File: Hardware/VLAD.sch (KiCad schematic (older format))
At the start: 29 parts, among them J1 BMP388, J2 BNO055, Q1 S8050, Q2 S8050, SW1 SW_Push, SW2 SW_Push, U1 ESP32-WROOM-32

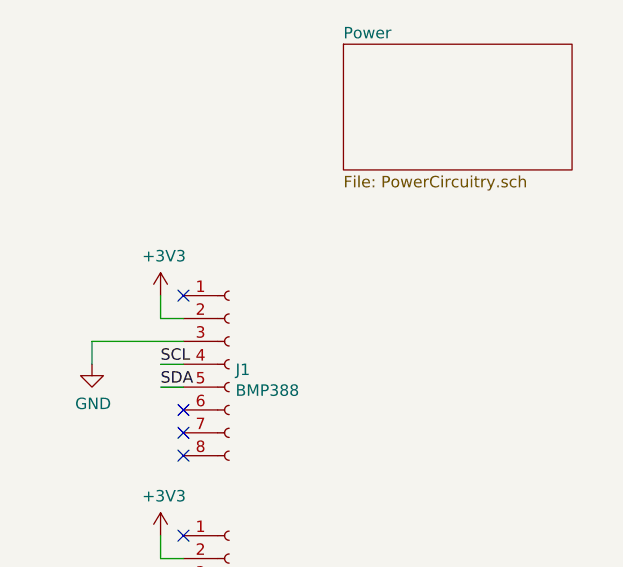
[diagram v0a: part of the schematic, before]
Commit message: Need to change pin headers for servo
Unsure at this stage, will look into which transistors etc to use.
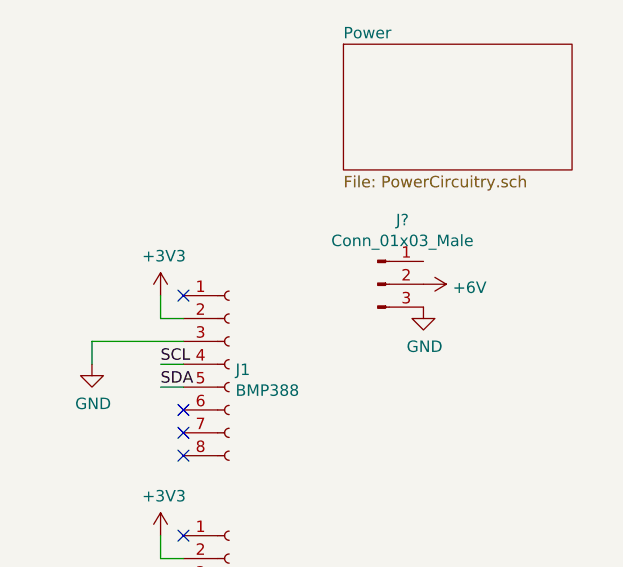
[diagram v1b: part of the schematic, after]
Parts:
- added J?: Conn_01x03_Male, symbol Connector:Conn_01x03_Male
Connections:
- net GND: now also J?.3 (Pin_3)
- new net +6V: J?.2 (Pin_2)
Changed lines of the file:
@@
 NoConn ~ 6750 4850
 NoConn ~ 7050 3950
+$Comp
+L power:+6V #PWR?
+U 1 1 60A0C2D4
+P 10200 2100
+F 0 "#PWR?" H 10200 1950 50  0001 C CNN
+F 1 "+6V" V 10215 2228 50  0000 L CNN
+F 2 "" H 10200 2100 50  0001 C CNN
+F 3 "" H 10200 2100 50  0001 C CNN
+	1    10200 2100
+	0    1    1    0
+$EndComp
+$Comp
+L power:GND #PWR?
+U 1 1 60A0B510
+P 10200 2200
+F 0 "#PWR?" H 10200 1950 50  0001 C CNN
+F 1 "GND" H 10205 2027 50  0000 C CNN
+F 2 "" H 10200 2200 50  0001 C CNN
+F 3 "" H 10200 2200 50  0001 C CNN
+	1    10200 2200
+	1    0    0    -1
+$EndComp
+$Comp
+L Connector:Conn_01x03_Male J?
+U 1 1 60A0527F
+P 10000 2100
+F 0 "J?" H 10108 2381 50  0000 C CNN
+F 1 "Conn_01x03_Male" H 10108 2290 50  0000 C CNN
+F 2 "" H 10000 2100 50  0001 C CNN
+F 3 "~" H 10000 2100 50  0001 C CNN
+	1    10000 2100
+	1    0    0    -1
+$EndComp
 $EndSCHEMATC

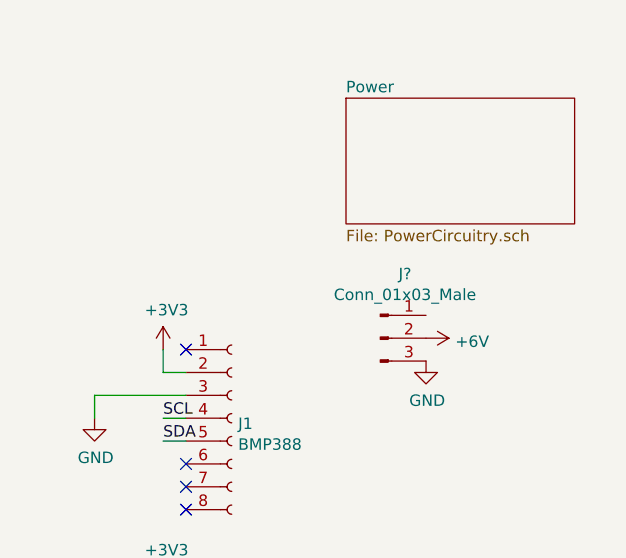
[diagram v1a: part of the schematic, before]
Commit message: Split PCB setup
Setup the PCB with each section split. J5 didn't have a schematic so I picked one.
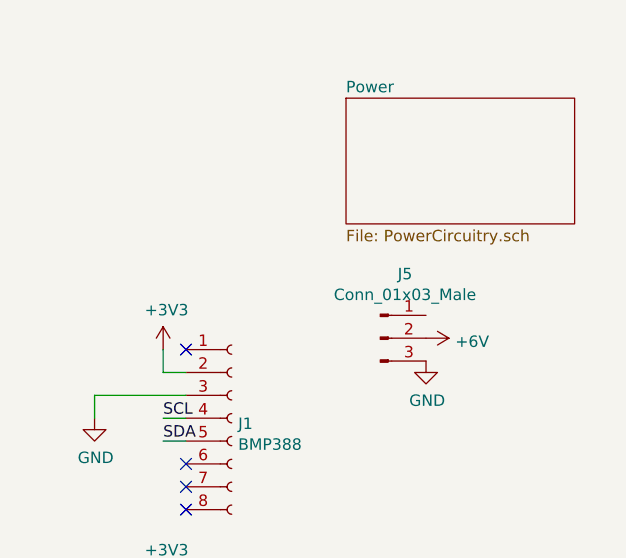
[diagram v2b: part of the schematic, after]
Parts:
- J5: renamed from J?; footprint (none) -> Connector_PinHeader_2.54mm:PinHeader_1x03_P2.54mm_Vertical
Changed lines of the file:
@@
 EESchema Schematic File Version 4
-LIBS:VLAD-cache
 EELAYER 30 0
 EELAYER END
@@
 NoConn ~ 7050 3950
 $Comp
-L power:+6V #PWR?
+L power:+6V #PWR0102
 U 1 1 60A0C2D4
 P 10200 2100
-F 0 "#PWR?" H 10200 1950 50  0001 C CNN
+F 0 "#PWR0102" H 10200 1950 50  0001 C CNN
 F 1 "+6V" V 10215 2228 50  0000 L CNN
 F 2 "" H 10200 2100 50  0001 C CNN
@@
 $EndComp
 $Comp
-L power:GND #PWR?
+L power:GND #PWR0103
 U 1 1 60A0B510
 P 10200 2200
-F 0 "#PWR?" H 10200 1950 50  0001 C CNN
+F 0 "#PWR0103" H 10200 1950 50  0001 C CNN
 F 1 "GND" H 10205 2027 50  0000 C CNN
 F 2 "" H 10200 2200 50  0001 C CNN
@@
 $EndComp
 $Comp
-L Connector:Conn_01x03_Male J?
+L Connector:Conn_01x03_Male J5
 U 1 1 60A0527F
 P 10000 2100
-F 0 "J?" H 10108 2381 50  0000 C CNN
+F 0 "J5" H 10108 2381 50  0000 C CNN
 F 1 "Conn_01x03_Male" H 10108 2290 50  0000 C CNN
-F 2 "" H 10000 2100 50  0001 C CNN
+F 2 "Connector_PinHeader_2.54mm:PinHeader_1x03_P2.54mm_Vertical" H 10000 2100 50  0001 C CNN
 F 3 "~" H 10000 2100 50  0001 C CNN
 	1    10000 2100

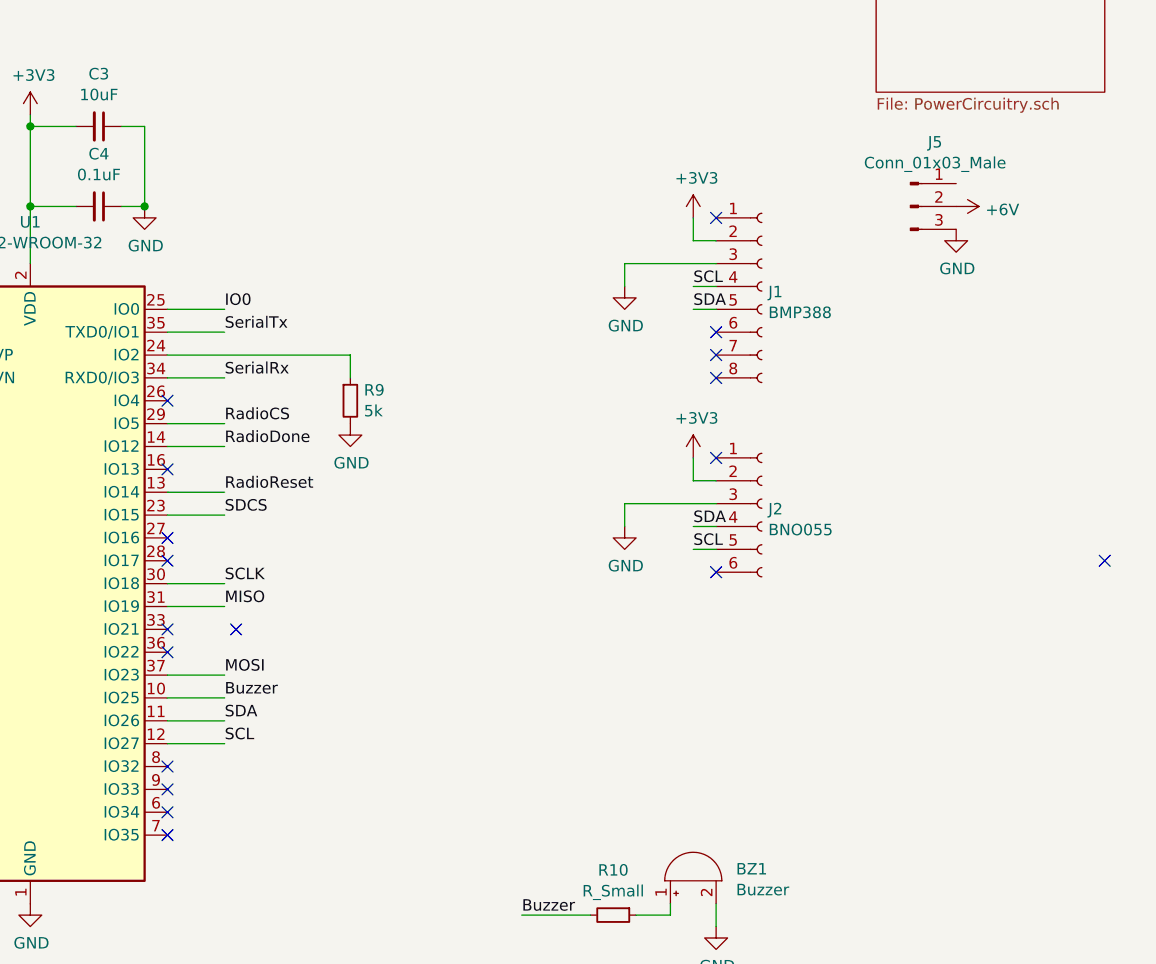
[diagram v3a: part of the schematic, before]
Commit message: Fixed N-Channel MOSFET, etc
And a few net label tings
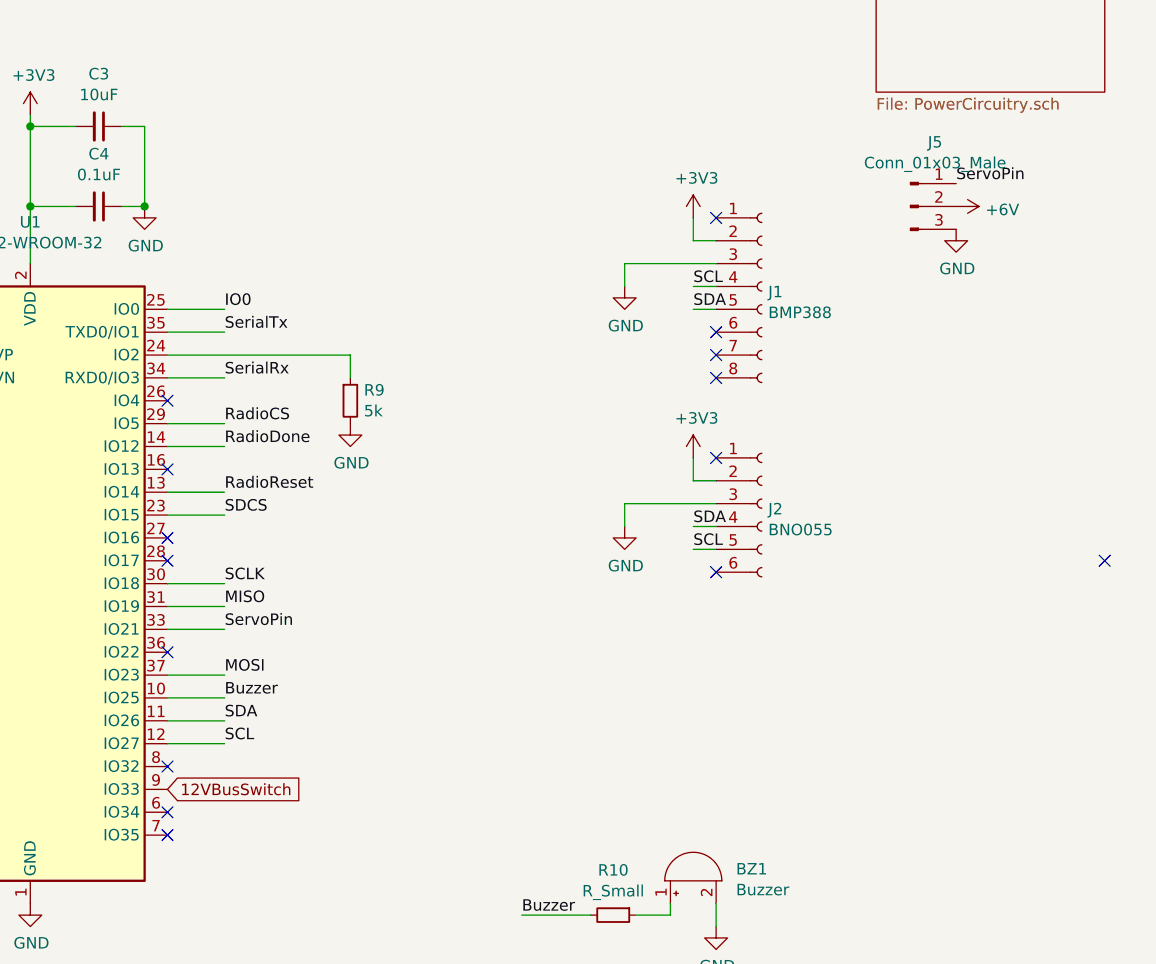
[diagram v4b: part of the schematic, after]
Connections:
- net ServoPin: now reaches U1.33 (IO21)
- net ServoPin: now also J5.1 (Pin_1)
- net 12VBusSwitch: now reaches U1.9 (IO33)
- no-connect marks 26 -> 23
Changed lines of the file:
@@
 $EndDescr
-$Comp
-L VLAD-rescue:ESP32-WROOM-32-RF_Module U1
-U 1 1 6068A42E
-P 6150 3750
-F 0 "U1" H 6150 5331 50  0000 C CNN
-F 1 "ESP32-WROOM-32" H 6150 5240 50  0000 C CNN
-F 2 "RF_Module:ESP32-WROOM-32" H 6150 2250 50  0001 C CNN
-F 3 "https://www.espressif.com/sites/default/files/documentation/esp32-wroom-32_datasheet_en.pdf" H 5850 3800 50  0001 C CNN
-	1    6150 3750
-	1    0    0    -1
-$EndComp
 $Comp
 L power:GND #PWR07
@@
 	1    0    0    -1
 $EndComp
-Wire Wire Line
-	6750 3750 7000 3750
-Wire Wire Line
-	6750 3850 7000 3850
-Wire Wire Line
-	6750 4150 7000 4150
 $Sheet
 S 800  1750 550  550
@@
 Text Label 1450 1000 0    50   ~ 0
 MOSI
-Wire Wire Line
-	6750 3150 7000 3150
 Text Label 7000 3150 0    50   ~ 0
 RadioDone
 Text Label 1450 1400 0    50   ~ 0
 RadioDone
-Wire Wire Line
-	6750 3350 7000 3350
 Text Label 7000 3350 0    50   ~ 0
 RadioReset
-Wire Wire Line
-	6750 3050 7000 3050
 Text Label 7000 3050 0    50   ~ 0
 RadioCS
@@
 Text Label 1450 2200 0    50   ~ 0
 SDCS
-Wire Wire Line
-	6750 3450 7000 3450
 Text Label 7000 3450 0    50   ~ 0
 SDCS
-Wire Wire Line
-	6750 2750 7550 2750
 Wire Wire Line
 	7550 2750 7550 2850
@@
 Wire Wire Line
 	6650 1750 6650 2100
-Wire Wire Line
-	6750 2850 7000 2850
-Wire Wire Line
-	6750 2650 7000 2650
 Text Label 7000 2850 0    50   ~ 0
 SerialRx
@@
 Text Label 8300 5200 0    50   ~ 0
 Buzzer
-Wire Wire Line
-	6750 4250 7000 4250
 Text Label 7000 4250 0    50   ~ 0
 Buzzer
-Wire Wire Line
-	6750 4350 7000 4350
-Wire Wire Line
-	6750 4450 7000 4450
 Text Label 7000 4350 0    50   ~ 0
 SDA
@@
 NoConn ~ 6750 3550
 NoConn ~ 6750 3650
-NoConn ~ 6750 3950
 NoConn ~ 6750 4050
-NoConn ~ 6750 4550
-NoConn ~ 6750 4650
-NoConn ~ 6750 4750
 NoConn ~ 6750 4850
-NoConn ~ 7050 3950
 $Comp
 L power:+6V #PWR0102
@@
 	1    0    0    -1
 $EndComp
+Wire Wire Line
+	6750 4450 7000 4450
+Wire Wire Line
+	6750 4350 7000 4350
+Wire Wire Line
+	6750 4250 7000 4250
+Wire Wire Line
+	6750 4150 7000 4150
+Wire Wire Line
+	6750 3850 7000 3850
+Wire Wire Line
+	6750 3750 7000 3750
+Wire Wire Line
+	6750 3450 7000 3450
+Wire Wire Line
+	6750 3350 7000 3350
+Wire Wire Line
+	6750 3150 7000 3150
+Wire Wire Line
+	6750 3050 7000 3050
+Wire Wire Line
+	6750 2850 7000 2850
+Wire Wire Line
+	6750 2750 7550 2750
+Wire Wire Line
+	6750 2650 7000 2650
+NoConn ~ 6750 4550
+$Comp
+L VLAD-rescue:ESP32-WROOM-32-RF_Module U1
+U 1 1 6068A42E
+P 6150 3750
+F 0 "U1" H 6150 5331 50  0000 C CNN
+F 1 "ESP32-WROOM-32" H 6150 5240 50  0000 C CNN
+F 2 "RF_Module:ESP32-WROOM-32" H 6150 2250 50  0001 C CNN
+F 3 "https://www.espressif.com/sites/default/files/documentation/esp32-wroom-32_datasheet_en.pdf" H 5850 3800 50  0001 C CNN
+	1    6150 3750
+	1    0    0    -1
+$EndComp
+Text GLabel 6750 4650 2    50   Input ~ 0
+12VBusSwitch
+NoConn ~ 6750 4750
+Text Label 7000 3950 0    50   ~ 0
+ServoPin
+Text Label 10200 2000 0    50   ~ 0
+ServoPin
+Wire Wire Line
+	6750 3950 7000 3950
 $EndSCHEMATC

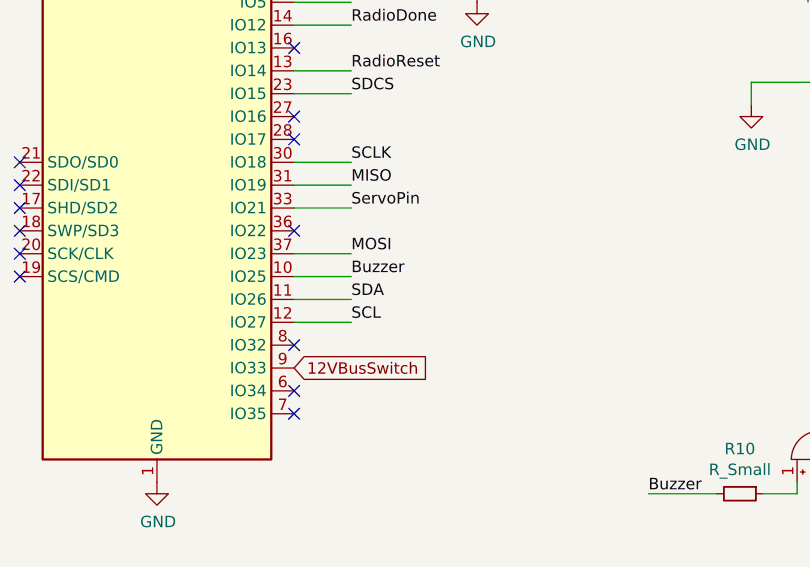
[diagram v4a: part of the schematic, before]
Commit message: Tracks done (albeit OCDifying)
All tracks are done in the sense that everything has found a routing, some components still may need to be moved though, such as the sensors on board and the push switches. 
Antenna stuff needs doing.
Board may need to be reshaped (keepout zone?).
GND plane needs to be added + silkscreens + memes
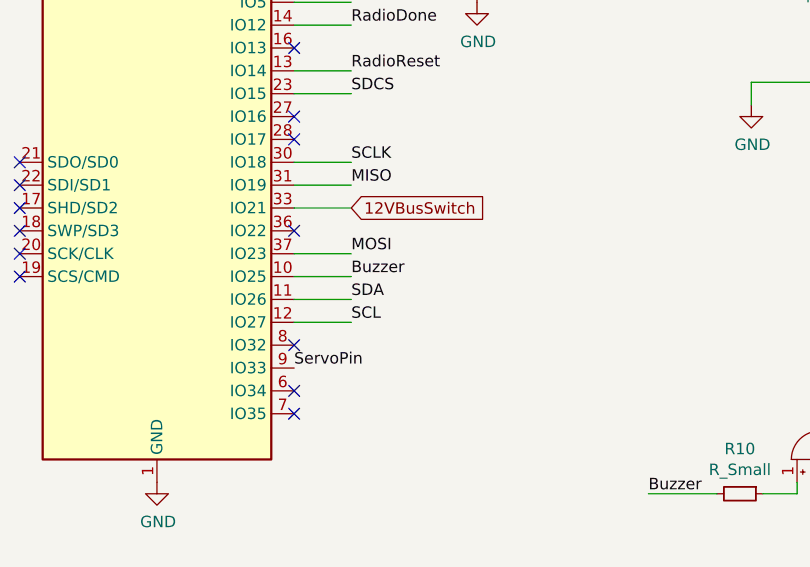
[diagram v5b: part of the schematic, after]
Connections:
- net 12VBusSwitch: now also U1.33 (IO21); no longer U1.9 (IO33)
- net ServoPin: now also U1.9 (IO33); no longer U1.33 (IO21)
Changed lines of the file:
@@
 	1    0    0    -1
 $EndComp
-Text GLabel 6750 4650 2    50   Input ~ 0
+Text GLabel 7000 3950 2    50   Input ~ 0
 12VBusSwitch
 NoConn ~ 6750 4750
-Text Label 7000 3950 0    50   ~ 0
+Text Label 6750 4650 0    50   ~ 0
 ServoPin
 Text Label 10200 2000 0    50   ~ 0

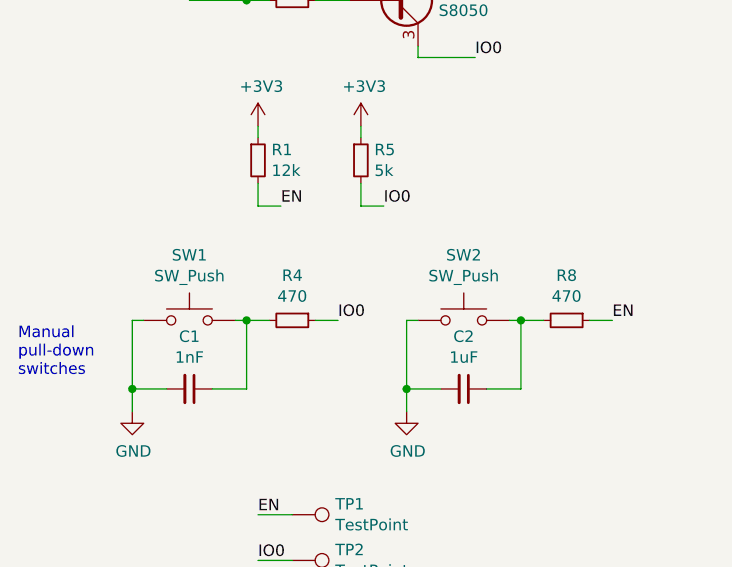
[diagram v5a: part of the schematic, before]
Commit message: Added GND plane and 3V3 plane
4 connections left to make, not sure what the issue is with some of them...
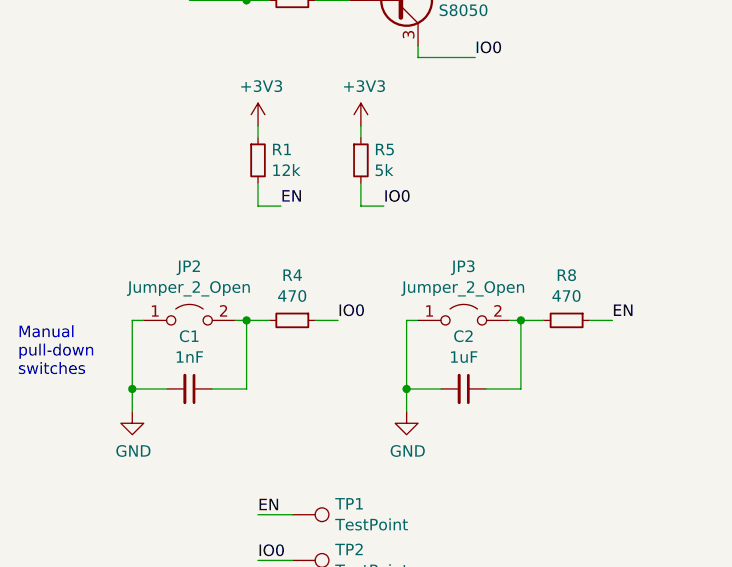
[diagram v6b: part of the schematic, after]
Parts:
- removed SW1, SW2: SW_Push, Button_Switch_SMD:SW_Push_1P1T_NO_6x6mm_H9.5mm, symbol Switch:SW_Push
- added JP2, JP3: Jumper_2_Open, Connector_PinHeader_2.54mm:PinHeader_1x02_P2.54mm_Vertical, symbol Jumper:Jumper_2_Open
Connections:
- net GND: now also JP2.1 (A), JP3.1 (A)
- net at C1.1, R4.2: now also JP2.2 (B)
- net at C2.1, R8.2: now also JP3.2 (B)
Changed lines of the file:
@@
 Wire Wire Line
 	2200 5700 2300 5700
-$Comp
-L Switch:SW_Push SW1
-U 1 1 609AA0D6
-P 1450 6200
-F 0 "SW1" H 1450 6485 50  0000 C CNN
-F 1 "SW_Push" H 1450 6394 50  0000 C CNN
-F 2 "Button_Switch_SMD:SW_Push_1P1T_NO_6x6mm_H9.5mm" H 1450 6400 50  0001 C CNN
-F 3 "~" H 1450 6400 50  0001 C CNN
-	1    1450 6200
-	1    0    0    -1
-$EndComp
 Wire Wire Line
 	1200 6200 1200 6500
@@
 Text Label 3300 6200 0    50   ~ 0
 EN
-$Comp
-L Switch:SW_Push SW2
-U 1 1 609D49CF
-P 2650 6200
-F 0 "SW2" H 2650 6485 50  0000 C CNN
-F 1 "SW_Push" H 2650 6394 50  0000 C CNN
-F 2 "Button_Switch_SMD:SW_Push_1P1T_NO_6x6mm_H9.5mm" H 2650 6400 50  0001 C CNN
-F 3 "~" H 2650 6400 50  0001 C CNN
-	1    2650 6200
-	1    0    0    -1
-$EndComp
 Text Notes 750  3700 0    50   ~ 0
 Auto Programmer, for how this works see this link:\nhttps://pcbartists.com/design/esp32-cp2102-programmer-schematic/
@@
 Wire Wire Line
 	6750 3950 7000 3950
+$Comp
+L Jumper:Jumper_2_Open JP2
+U 1 1 60B2C548
+P 1450 6200
+F 0 "JP2" H 1450 6435 50  0000 C CNN
+F 1 "Jumper_2_Open" H 1450 6344 50  0000 C CNN
+F 2 "Connector_PinHeader_2.54mm:PinHeader_1x02_P2.54mm_Vertical" H 1450 6200 50  0001 C CNN
+F 3 "~" H 1450 6200 50  0001 C CNN
+	1    1450 6200
+	1    0    0    -1
+$EndComp
+$Comp
+L Jumper:Jumper_2_Open JP3
+U 1 1 60B2CD42
+P 2650 6200
+F 0 "JP3" H 2650 6435 50  0000 C CNN
+F 1 "Jumper_2_Open" H 2650 6344 50  0000 C CNN
+F 2 "Connector_PinHeader_2.54mm:PinHeader_1x02_P2.54mm_Vertical" H 2650 6200 50  0001 C CNN
+F 3 "~" H 2650 6200 50  0001 C CNN
+	1    2650 6200
+	1    0    0    -1
+$EndComp
 $EndSCHEMATC

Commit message: Tried to add footprints. Emphasis on tried.
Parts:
- removed Q1, Q2: S8050, Package_TO_SOT_THT:TO-92_Inline, symbol Transistor_BJT:S8050
- added Q1, Q2: MMDT2222A, Package_TO_SOT_SMD:SOT-363_SC-70-6, symbol Transistor_BJT:MMDT2222A
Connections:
- net EN: now also Q1.1 (E1)
- net IO0: now also Q2.6 (C1)
- net USB_DTR: now also Q2.1 (E1)
- net USB_RTS: now also Q1.6 (C1)
- net at R2.1: now also Q1.2 (B1)
- net at R3.1: now also Q2.2 (B1)
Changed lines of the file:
@@
 SerialRx
-$Comp
-L Transistor_BJT:S8050 Q1
-U 1 1 6093351E
-P 2350 4100
-F 0 "Q1" H 2540 4146 50  0000 L CNN
-F 1 "S8050" H 2540 4055 50  0000 L CNN
-F 2 "Package_TO_SOT_THT:TO-92_Inline" H 2550 4025 50  0001 L CIN
-F 3 "http://www.unisonic.com.tw/datasheet/S8050.pdf" H 2350 4100 50  0001 L CNN
-	1    2350 4100
-	1    0    0    -1
-$EndComp
-$Comp
-L Transistor_BJT:S8050 Q2
-U 1 1 60938289
-P 2350 4800
-F 0 "Q2" H 2540 4754 50  0000 L CNN
-F 1 "S8050" H 2540 4845 50  0000 L CNN
-F 2 "Package_TO_SOT_THT:TO-92_Inline" H 2550 4725 50  0001 L CIN
-F 3 "http://www.unisonic.com.tw/datasheet/S8050.pdf" H 2350 4800 50  0001 L CNN
-	1    2350 4800
-	1    0    0    1
-$EndComp
 $Comp
 L Device:R_Small R2
@@
 	1    0    0    -1
 $EndComp
+$Comp
+L Transistor_BJT:MMDT2222A Q2
+U 1 1 60B6FFE0
+P 2350 4800
+F 0 "Q2" H 2540 4754 50  0000 L CNN
+F 1 "MMDT2222A" H 2540 4845 50  0000 L CNN
+F 2 "Package_TO_SOT_SMD:SOT-363_SC-70-6" H 2550 4900 50  0001 C CNN
+F 3 "http://www.diodes.com/_files/datasheets/ds30125.pdf" H 2350 4800 50  0001 C CNN
+	1    2350 4800
+	1    0    0    1
+$EndComp
+$Comp
+L Transistor_BJT:MMDT2222A Q1
+U 1 1 60B80B3B
+P 2350 4100
+F 0 "Q1" H 2540 4054 50  0000 L CNN
+F 1 "MMDT2222A" H 2540 4145 50  0000 L CNN
+F 2 "Package_TO_SOT_SMD:SOT-363_SC-70-6" H 2550 4200 50  0001 C CNN
+F 3 "http://www.diodes.com/_files/datasheets/ds30125.pdf" H 2350 4100 50  0001 C CNN
+	1    2350 4100
+	1    0    0    1
+$EndComp
 $EndSCHEMATC
